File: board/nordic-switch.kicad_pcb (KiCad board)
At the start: 2 copper layers, 24 x 53 mm, 37 parts, among them J1 Screw_Terminal_01x01, J2 Screw_Terminal_01x01, J3 Screw_Terminal_01x01, J4 Screw_Terminal_01x01, J5 Conn_Coaxial, SW1 SW_Push, U1 nRF52832-QFxx, Y1 Crystal_GND24

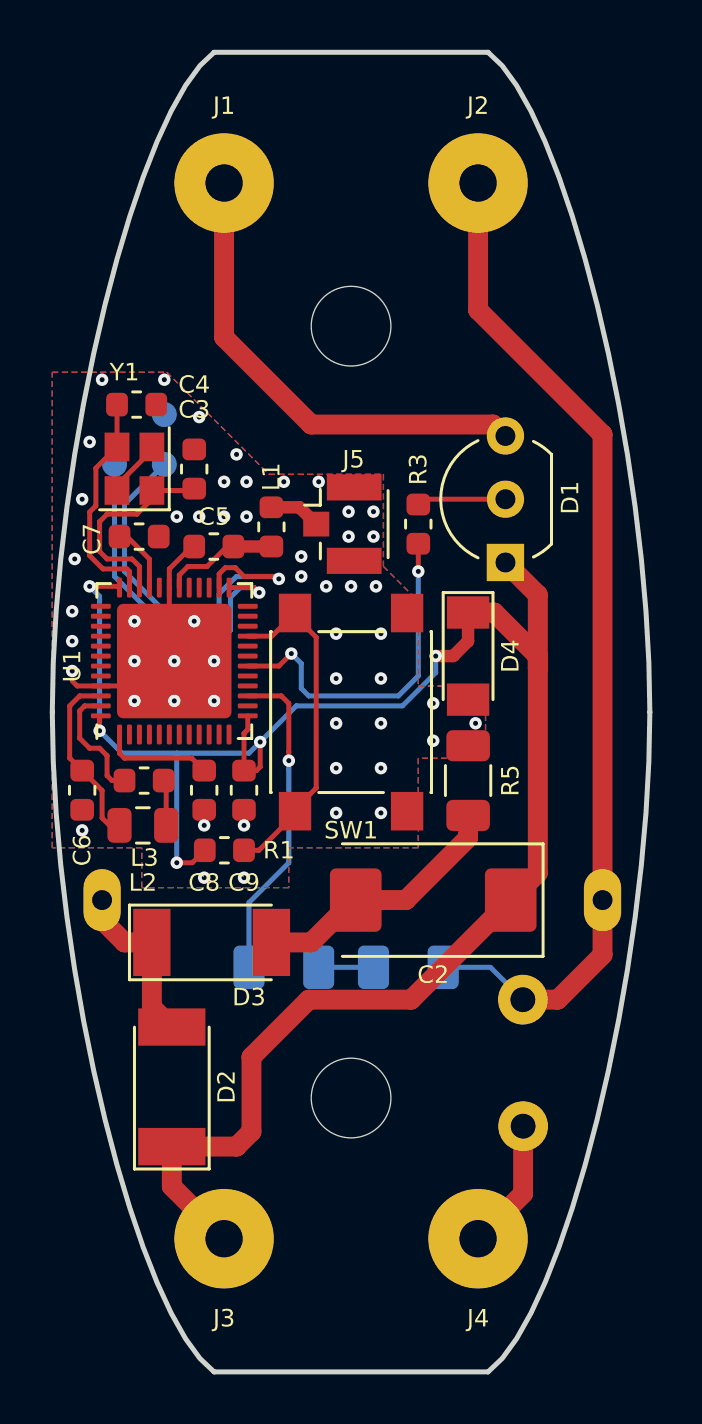
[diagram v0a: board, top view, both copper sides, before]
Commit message: PCB version 1.1
- Switched to Kicad 8
- Better spacing for the high-voltage part
- Re-route SWD from crystal area
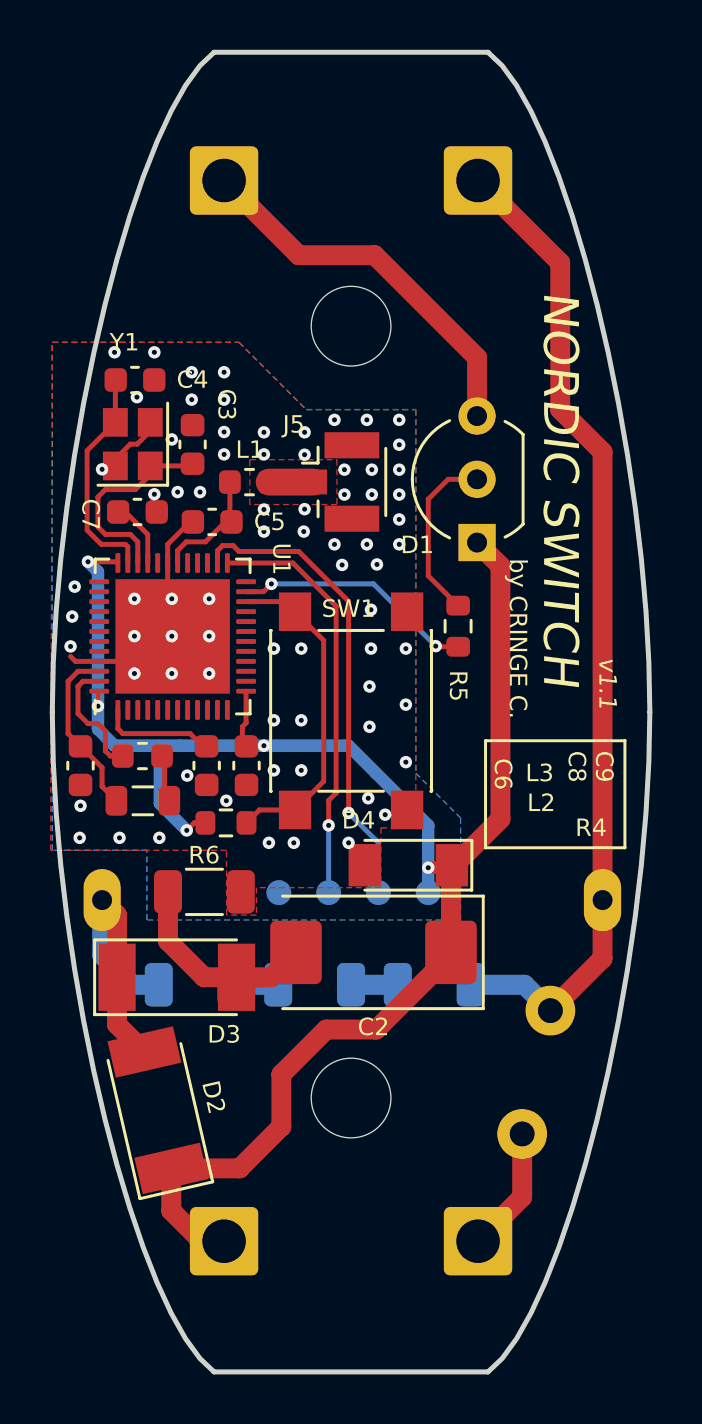
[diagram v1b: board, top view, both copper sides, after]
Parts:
- removed the R4 at (141.7, 110.0)
- removed REF**: OSHW-Logo2_7.3x6mm_SilkScreen, Symbol:OSHW-Logo2_7.3x6mm_SilkScreen
- added R1: 470K, Resistor_SMD:R_1206_3216Metric, B.Cu at (147.7, 110.7)
- added R3: 470K, Resistor_SMD:R_1206_3216Metric, B.Cu at (138.1, 110.7)
- added TP3: VCC, TestPoint:TestPoint_Pad_D1.0mm, B.Cu at (147.5, 107.0)
- C1: value 680n -> 680n 400V
- C2: value 100uf -> 330uF 16V
- C5: value 1pF -> 0.8pF
- F1: value 1A -> 0.7A
- J1: renamed from J3; footprint Connector_Wire:SolderWirePad_1x01_Drill1.5mm -> Connector_Wire:SolderWire-1sqmm_1x01_D1.4mm_OD2.7mm
- J2: renamed from J4; footprint Connector_Wire:SolderWirePad_1x01_Drill1.5mm -> Connector_Wire:SolderWire-1sqmm_1x01_D1.4mm_OD2.7mm
- J3: renamed from J1; footprint Connector_Wire:SolderWirePad_1x01_Drill1.5mm -> Connector_Wire:SolderWire-1sqmm_1x01_D1.4mm_OD2.7mm
- J4: renamed from J2; footprint Connector_Wire:SolderWirePad_1x01_Drill1.5mm -> Connector_Wire:SolderWire-1sqmm_1x01_D1.4mm_OD2.7mm
- J5: value Conn_Coaxial -> IPX
- L1: value 3.3nH -> 3.9nH
- SW1: value SW_Push -> Control
- moved TP4 19.7 mm to (141.5, 107.0)
- moved TP1 19.2 mm to (143.5, 107.0)
- moved TP2 19.2 mm to (145.5, 107.0)
- moved R6 11.5 mm to (138.5, 107.0), turned to 180 degrees
- moved D4 8.74 mm to (146.7, 105.9), turned to 180 degrees
- moved R5 4.40 mm to (148.7, 96.3)
- moved R2 3.83 mm to (142.9, 110.7)
- moved C2 3.19 mm to (145.3, 109.4)
- moved L1 2.00 mm to (140.3, 90.5), turned to 0 degrees
- moved D3 1.98 mm to (137.4, 110.4)
- moved J5 1.69 mm to (144.0, 90.5)
- moved D1 1.39 mm to (149.5, 92.9)
- moved F1 1.19 mm to (152.4, 111.7), turned to -103 degrees
- moved R4 1.10 mm to (139.4, 104.2)
- moved D2 1.09 mm to (136.6, 115.7), turned to 103 degrees
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- renumbered R1 to R4, R3 to R5, R5 to R6, TP3 to TP4
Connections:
- net Net-(J5-Pad1) renamed /ANT_IMP_MATCHED
- C1 pad 1: Net-(C1-Pad1) -> Net-(J4-Pin_1)
- F1 pad 1: Net-(C1-Pad1) -> Net-(J4-Pin_1)
- J4 pad 1: Net-(C1-Pad1) -> Net-(J4-Pin_1)
- R2 pad 2: Net-(C1-Pad1) -> Net-(R1-Pad1)
- R4 pad 1: /BUTTON -> /PUSH_BUTTON
- SW1 pad 2: /BUTTON -> /PUSH_BUTTON
- U1 pad 10: Net-(U1-Pad10) -> unconnected-(U1-P0.08-Pad10)
- U1 pad 11: Net-(U1-Pad11) -> unconnected-(U1-NFC1/P0.09-Pad11)
- U1 pad 12: Net-(U1-Pad12) -> unconnected-(U1-NFC2/P0.10-Pad12)
- U1 pad 14: Net-(U1-Pad14) -> unconnected-(U1-P0.11-Pad14)
- U1 pad 15: /ZERO_CROSS -> unconnected-(U1-P0.12-Pad15)
- U1 pad 16: Net-(U1-Pad16) -> unconnected-(U1-P0.13-Pad16)
- U1 pad 17: Net-(U1-Pad17) -> unconnected-(U1-P0.14-Pad17)
- U1 pad 18: /TRIAC_GATE -> unconnected-(U1-P0.15-Pad18)
- U1 pad 19: Net-(U1-Pad19) -> unconnected-(U1-P0.16-Pad19)
- U1 pad 2: Net-(U1-Pad2) -> unconnected-(U1-P0.00/XL1-Pad2)
- U1 pad 20: Net-(U1-Pad20) -> unconnected-(U1-P0.17-Pad20)
- U1 pad 21: /BUTTON -> unconnected-(U1-P0.18/SWO-Pad21)
- U1 pad 22: Net-(U1-Pad22) -> /PUSH_BUTTON
- U1 pad 23: Net-(U1-Pad23) -> /TRIAC_GATE
- U1 pad 24: Net-(U1-Pad24) -> unconnected-(U1-P0.21/~{RESET}-Pad24)
- U1 pad 27: Net-(U1-Pad27) -> unconnected-(U1-P0.22-Pad27)
- U1 pad 28: Net-(U1-Pad28) -> unconnected-(U1-P0.23-Pad28)
- U1 pad 29: Net-(U1-Pad29) -> unconnected-(U1-P0.24-Pad29)
- U1 pad 3: Net-(U1-Pad3) -> unconnected-(U1-P0.01/XL2-Pad3)
- U1 pad 32: Net-(U1-Pad32) -> unconnected-(U1-DEC2-Pad32)
- U1 pad 37: Net-(U1-Pad37) -> unconnected-(U1-P0.25-Pad37)
- U1 pad 38: Net-(U1-Pad38) -> unconnected-(U1-P0.26-Pad38)
- U1 pad 39: Net-(U1-Pad39) -> unconnected-(U1-P0.27-Pad39)
- U1 pad 4: Net-(U1-Pad4) -> unconnected-(U1-P0.02/AIN0-Pad4)
- U1 pad 40: Net-(U1-Pad40) -> unconnected-(U1-P0.28/AIN4-Pad40)
- U1 pad 41: Net-(U1-Pad41) -> unconnected-(U1-P0.29/AIN5-Pad41)
- U1 pad 42: Net-(U1-Pad42) -> unconnected-(U1-P0.30/AIN6-Pad42)
- U1 pad 43: Net-(U1-Pad43) -> unconnected-(U1-P0.31/AIN7-Pad43)
- U1 pad 44: Net-(U1-Pad44) -> unconnected-(U1-NC-Pad44)
- U1 pad 5: Net-(U1-Pad5) -> unconnected-(U1-P0.03/AIN1-Pad5)
- U1 pad 6: Net-(U1-Pad6) -> unconnected-(U1-P0.04/AIN2-Pad6)
- U1 pad 7: Net-(U1-Pad7) -> unconnected-(U1-P0.05/AIN3-Pad7)
- U1 pad 8: Net-(U1-Pad8) -> unconnected-(U1-P0.06-Pad8)
- U1 pad 9: Net-(U1-Pad9) -> unconnected-(U1-P0.07-Pad9)
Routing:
- net Net-(C1-Pad1): track 40.8 -> 0.00 mm
- net Net-(J4-Pin_1): track 0.00 -> 39.9 mm
- net /BUTTON: track 13.7 -> 0.00 mm
- net /PUSH_BUTTON: track 0.00 -> 13.2 mm
- net /ZERO_CROSS: track 13.0 -> 0.00 mm, vias 1 -> 0
- net +3V3: track 78.7 -> 73.6 mm
- net Net-(D2-A): track 6.90 -> 11.8 mm
- net /TRIAC_GATE: track 14.0 -> 9.69 mm
- net Net-(D1-A2): track 19.2 -> 15.5 mm
- net Net-(D1-G): track 3.59 -> 7.06 mm
- net Net-(D3-A): track 10.4 -> 8.13 mm
- net Net-(R1-Pad1): track 0.00 -> 1.88 mm
- net /SWDCLK: track 15.0 -> 16.7 mm
- net /SWDIO: track 17.8 -> 19.0 mm
- net GND: vias 53 -> 74
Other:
- net class Default removed
- rule pad_to_mask_clearance: 0.051 -> 0
- board text added: "0.7A MAX"
- board text added: "C"
- board text added: "D"
- board text added: "G"
- board text added: "NORDIC SWITCH"
- board text added: "Never debug while live!"
- board text added: "V"
- board text added: "by CRINGE C."
- board text added: "v1.1"
- board text removed: "Nordic- switch 1.0"

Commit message: drop gerbers, docs, archives...
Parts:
- C1: value 680n 400V -> 220n 600V
- C2: value 330uF 16V -> 220uF 10V
- R4: value 10k -> 100k
- R5: value 680 -> 1K
- R6: value 510 -> 51R
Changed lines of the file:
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@@
 			)
 		)
-		(property "Value" "330uF 16V"
+		(property "Value" "220uF 10V"
 			(at 0 3.1 0)
 			(unlocked yes)
@@
 			)
 		)
-		(property "Value" "510"
+		(property "Value" "51R"
 			(at 0 1.82 0)
 			(unlocked yes)
@@
 			)
 		)
-		(property "Value" "680"
+		(property "Value" "1K"
 			(at 0 1.43 90)
 			(unlocked yes)
@@
 			)
 		)
-		(property "Value" "10k"
+		(property "Value" "100k"
 			(at 0 1.43 0)
 			(unlocked yes)
@@
 		(sheetname "Root")
 		(sheetfile "nordic-switch.kicad_sch")
-		(attr smd)
+		(attr smd dnp)
 		(fp_line
 			(start -0.237258 0.5225)
@@
 			)
 		)
-		(property "Value" "680n 400V"
+		(property "Value" "220n 600V"
 			(at -1.6 -2.575 180)
 			(unlocked yes)
